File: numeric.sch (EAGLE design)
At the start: 28 parts, among them IC1 MEGA8-AI, Q2 BC817-16SMD, Q3 BC817-16SMD, SW2 EC12E_SW

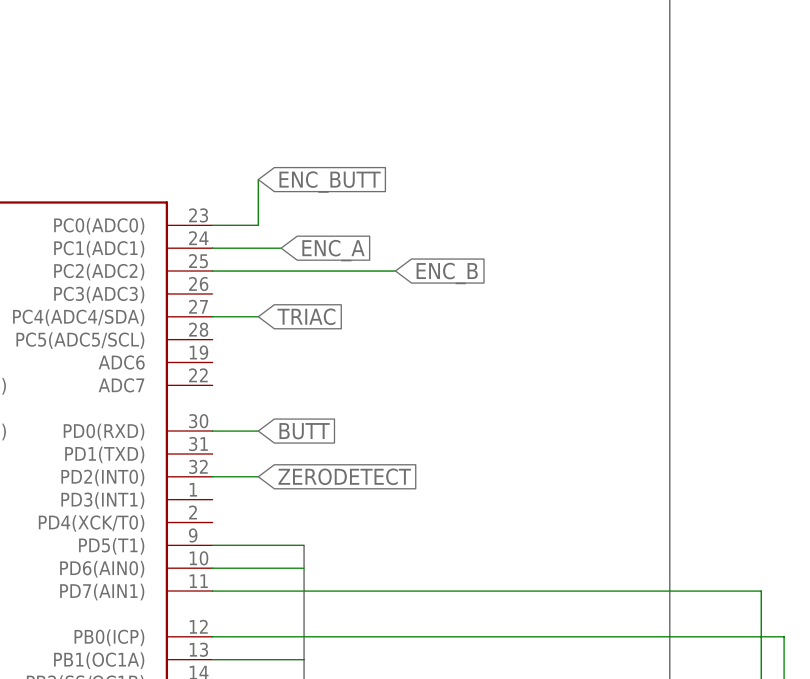
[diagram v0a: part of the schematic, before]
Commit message: Добавил разводку на горизонтальную плату
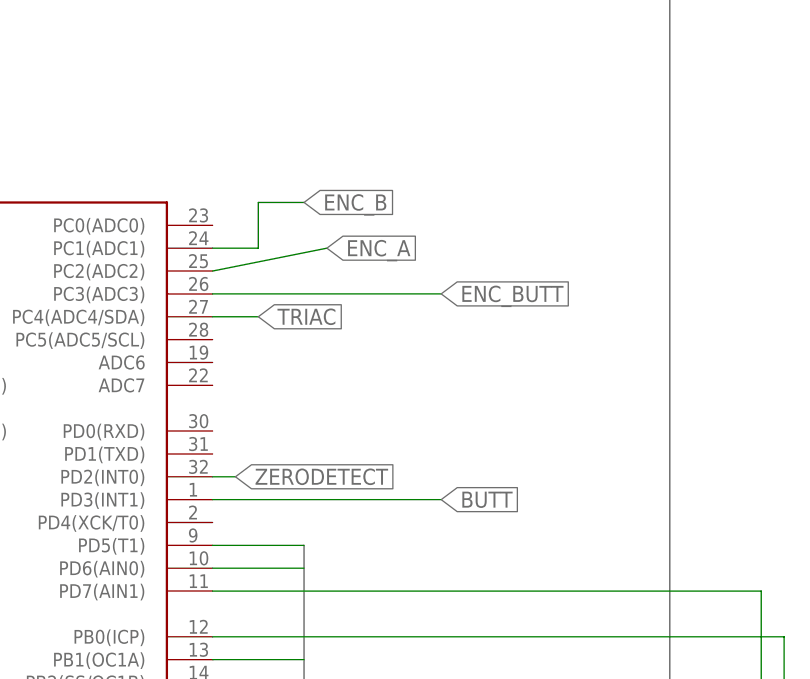
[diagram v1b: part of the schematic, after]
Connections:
- net N$1 renamed BASE_Q3
- net N$13 renamed RESET
- net N$2 renamed BASE_Q2
- net BUTT: now also IC1.PD3(INT1); no longer IC1.PD0(RXD)
- net ENC_A: now also IC1.PC2(ADC2); no longer IC1.PC1(ADC1)
- net ENC_B: now also IC1.PC1(ADC1); no longer IC1.PC2(ADC2)
- net ENC_BUTT: now also IC1.PC3(ADC3); no longer IC1.PC0(ADC0)
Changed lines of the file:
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@@
 <net name="ZERODETECT" class="0">
-<segment>
-<pinref part="IC1" gate="G$1" pin="PD2(INT0)"/>
-<wire x1="7.62" y1="111.76" x2="12.7" y2="111.76" width="0.1524" layer="91"/>
-<label x="12.7" y="111.76" size="1.778" layer="95" xref="yes"/>
-</segment>
 <segment>
 <pinref part="R5" gate="G$1" pin="1"/>
@@
 <pinref part="TO_4N33" gate="G$1" pin="2"/>
 <wire x1="-83.82" y1="5.08" x2="-66.04" y2="5.08" width="0.1524" layer="91"/>
+</segment>
+<segment>
+<pinref part="IC1" gate="G$1" pin="PD2(INT0)"/>
+<wire x1="7.62" y1="111.76" x2="10.16" y2="111.76" width="0.1524" layer="91"/>
+<label x="10.16" y="111.76" size="1.778" layer="95" xref="yes"/>
 </segment>
 </net>
@@
 </segment>
 </net>
-<net name="N$13" class="0">
+<net name="RESET" class="0">
 <segment>
 <pinref part="R11" gate="G$1" pin="1"/>
@@
 </segment>
 <segment>
-<label x="27.94" y="134.62" size="1.778" layer="95" xref="yes"/>
-<pinref part="IC1" gate="G$1" pin="PC2(ADC2)"/>
-<wire x1="7.62" y1="134.62" x2="27.94" y2="134.62" width="0.1524" layer="91"/>
+<pinref part="IC1" gate="G$1" pin="PC1(ADC1)"/>
+<wire x1="7.62" y1="137.16" x2="12.7" y2="137.16" width="0.1524" layer="91"/>
+<label x="17.78" y="142.24" size="1.778" layer="95" xref="yes"/>
+<wire x1="12.7" y1="137.16" x2="12.7" y2="142.24" width="0.1524" layer="91"/>
+<wire x1="12.7" y1="142.24" x2="17.78" y2="142.24" width="0.1524" layer="91"/>
 </segment>
 </net>
@@
 </segment>
 <segment>
-<wire x1="7.62" y1="137.16" x2="15.24" y2="137.16" width="0.1524" layer="91"/>
-<label x="15.24" y="137.16" size="1.778" layer="95" xref="yes"/>
-<pinref part="IC1" gate="G$1" pin="PC1(ADC1)"/>
+<pinref part="IC1" gate="G$1" pin="PC2(ADC2)"/>
+<wire x1="7.62" y1="134.62" x2="20.32" y2="137.16" width="0.1524" layer="91"/>
+<label x="20.32" y="137.16" size="1.778" layer="95" xref="yes"/>
 </segment>
 </net>
@@
 </segment>
 <segment>
-<label x="12.7" y="144.78" size="1.778" layer="95" xref="yes"/>
-<wire x1="12.7" y1="139.7" x2="12.7" y2="144.78" width="0.1524" layer="91"/>
-<pinref part="IC1" gate="G$1" pin="PC0(ADC0)"/>
-<wire x1="12.7" y1="139.7" x2="7.62" y2="139.7" width="0.1524" layer="91"/>
+<pinref part="IC1" gate="G$1" pin="PC3(ADC3)"/>
+<wire x1="7.62" y1="132.08" x2="33.02" y2="132.08" width="0.1524" layer="91"/>
+<label x="33.02" y="132.08" size="1.778" layer="95" xref="yes"/>
 </segment>
 </net>
@@
 </segment>
 <segment>
-<pinref part="IC1" gate="G$1" pin="PD0(RXD)"/>
-<wire x1="7.62" y1="116.84" x2="12.7" y2="116.84" width="0.1524" layer="91"/>
-<label x="12.7" y="116.84" size="1.778" layer="95" xref="yes"/>
+<pinref part="IC1" gate="G$1" pin="PD3(INT1)"/>
+<wire x1="7.62" y1="109.22" x2="33.02" y2="109.22" width="0.1524" layer="91"/>
+<label x="33.02" y="109.22" size="1.778" layer="95" xref="yes"/>
 </segment>
 </net>
@@
 </segment>
 </net>
-<net name="N$1" class="0">
+<net name="BASE_Q3" class="0">
 <segment>
 <pinref part="R19" gate="G$1" pin="2"/>
@@
 </segment>
 </net>
-<net name="N$2" class="0">
+<net name="BASE_Q2" class="0">
 <segment>
 <pinref part="R17" gate="G$1" pin="2"/>

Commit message: Провел проверку DRC
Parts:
- C2, C3: device rcl:C-EUC1210K -> rcl:C-EUC1206K
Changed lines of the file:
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@@
 <grid distance="0.1" unitdist="inch" unit="inch" style="lines" multiple="1" display="no" altdistance="0.01" altunitdist="inch" altunit="inch"/>
 <layers>
-<layer number="1" name="Top" color="4" fill="1" visible="no" active="no"/>
-<layer number="16" name="Bottom" color="1" fill="1" visible="no" active="no"/>
-<layer number="17" name="Pads" color="2" fill="1" visible="no" active="no"/>
-<layer number="18" name="Vias" color="2" fill="1" visible="no" active="no"/>
-<layer number="19" name="Unrouted" color="6" fill="1" visible="no" active="no"/>
-<layer number="20" name="Dimension" color="15" fill="1" visible="no" active="no"/>
-<layer number="21" name="tPlace" color="7" fill="1" visible="no" active="no"/>
-<layer number="22" name="bPlace" color="7" fill="1" visible="no" active="no"/>
-<layer number="23" name="tOrigins" color="15" fill="1" visible="no" active="no"/>
-<layer number="24" name="bOrigins" color="15" fill="1" visible="no" active="no"/>
-<layer number="25" name="tNames" color="7" fill="1" visible="no" active="no"/>
-<layer number="26" name="bNames" color="7" fill="1" visible="no" active="no"/>
-<layer number="27" name="tValues" color="7" fill="1" visible="no" active="no"/>
-<layer number="28" name="bValues" color="7" fill="1" visible="no" active="no"/>
+<layer number="1" name="Top" color="4" fill="1" visible="yes" active="no"/>
+<layer number="16" name="Bottom" color="1" fill="1" visible="yes" active="no"/>
+<layer number="17" name="Pads" color="2" fill="1" visible="yes" active="no"/>
+<layer number="18" name="Vias" color="2" fill="1" visible="yes" active="no"/>
+<layer number="19" name="Unrouted" color="6" fill="1" visible="yes" active="no"/>
+<layer number="20" name="Dimension" color="15" fill="1" visible="yes" active="no"/>
+<layer number="21" name="tPlace" color="7" fill="1" visible="yes" active="no"/>
+<layer number="22" name="bPlace" color="7" fill="1" visible="yes" active="no"/>
+<layer number="23" name="tOrigins" color="15" fill="1" visible="yes" active="no"/>
+<layer number="24" name="bOrigins" color="15" fill="1" visible="yes" active="no"/>
+<layer number="25" name="tNames" color="7" fill="1" visible="yes" active="no"/>
+<layer number="26" name="bNames" color="7" fill="1" visible="yes" active="no"/>
+<layer number="27" name="tValues" color="7" fill="1" visible="yes" active="no"/>
+<layer number="28" name="bValues" color="7" fill="1" visible="yes" active="no"/>
 <layer number="29" name="tStop" color="7" fill="3" visible="no" active="no"/>
 <layer number="30" name="bStop" color="7" fill="6" visible="no" active="no"/>
@@
 <layer number="35" name="tGlue" color="7" fill="4" visible="no" active="no"/>
 <layer number="36" name="bGlue" color="7" fill="5" visible="no" active="no"/>
-<layer number="37" name="tTest" color="7" fill="1" visible="no" active="no"/>
-<layer number="38" name="bTest" color="7" fill="1" visible="no" active="no"/>
+<layer number="37" name="tTest" color="7" fill="1" visible="yes" active="no"/>
+<layer number="38" name="bTest" color="7" fill="1" visible="yes" active="no"/>
 <layer number="39" name="tKeepout" color="4" fill="11" visible="no" active="no"/>
 <layer number="40" name="bKeepout" color="1" fill="11" visible="no" active="no"/>
@@
 <layer number="44" name="Drills" color="7" fill="1" visible="no" active="no"/>
 <layer number="45" name="Holes" color="7" fill="1" visible="no" active="no"/>
-<layer number="46" name="Milling" color="3" fill="1" visible="no" active="no"/>
-<layer number="47" name="Measures" color="7" fill="1" visible="no" active="no"/>
-<layer number="48" name="Document" color="7" fill="1" visible="no" active="no"/>
-<layer number="49" name="Reference" color="7" fill="1" visible="no" active="no"/>
-<layer number="50" name="dxf" color="7" fill="1" visible="no" active="no"/>
-<layer number="51" name="tDocu" color="7" fill="1" visible="no" active="no"/>
-<layer number="52" name="bDocu" color="7" fill="1" visible="no" active="no"/>
+<layer number="46" name="Milling" color="3" fill="1" visible="yes" active="no"/>
+<layer number="47" name="Measures" color="7" fill="1" visible="yes" active="no"/>
+<layer number="48" name="Document" color="7" fill="1" visible="yes" active="no"/>
+<layer number="49" name="Reference" color="7" fill="1" visible="yes" active="no"/>
+<layer number="50" name="dxf" color="7" fill="1" visible="yes" active="no"/>
+<layer number="51" name="tDocu" color="7" fill="1" visible="yes" active="no"/>
+<layer number="52" name="bDocu" color="7" fill="1" visible="yes" active="no"/>
 <layer number="90" name="Modules" color="5" fill="1" visible="yes" active="yes"/>
 <layer number="91" name="Nets" color="2" fill="1" visible="yes" active="yes"/>
@@
 <part name="R11" library="rcl" deviceset="R-US_" device="M1206" value="4.7k"/>
 <part name="P+4" library="supply1" deviceset="+5V" device=""/>
-<part name="C2" library="rcl" deviceset="C-EU" device="C1210K"/>
+<part name="C2" library="rcl" deviceset="C-EU" device="C1206K"/>
 <part name="GND5" library="supply1" deviceset="GND" device=""/>
-<part name="C3" library="rcl" deviceset="C-EU" device="C1210K"/>
+<part name="C3" library="rcl" deviceset="C-EU" device="C1206K"/>
 <part name="R12" library="rcl" deviceset="R-US_" device="M1206" value="360"/>
 <part name="R13" library="rcl" deviceset="R-US_" device="M1206" value="360"/>
